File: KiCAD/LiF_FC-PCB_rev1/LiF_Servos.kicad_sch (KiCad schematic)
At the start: 4 parts, among them J37 SRV 3V3_{EN}, J38 Servo A, J39 Servo B

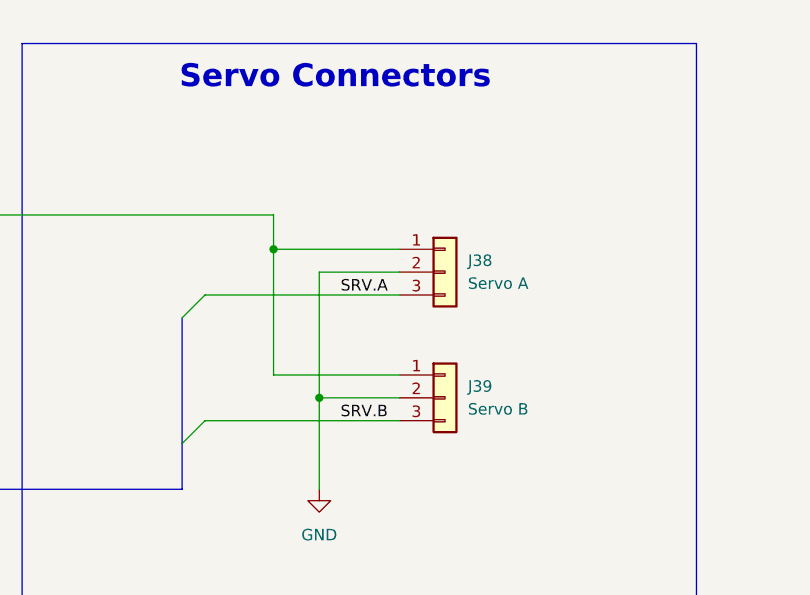
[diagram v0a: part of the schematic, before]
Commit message: fixing ERC bugs on schematic. Only MCU left
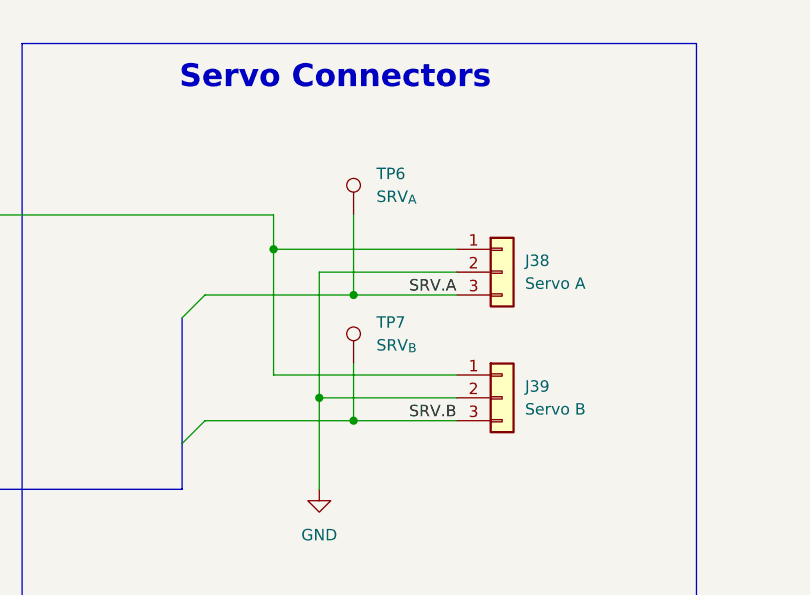
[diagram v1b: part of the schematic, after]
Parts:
- added TP6: SRV_{A}, TestPoint:TestPoint_Bridge_Pitch2.54mm_Drill1.0mm, symbol Connector:TestPoint
- added TP7: SRV_{B}, TestPoint:TestPoint_Bridge_Pitch2.54mm_Drill1.0mm, symbol Connector:TestPoint
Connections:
- net SRV.A: now also TP6.1
- net SRV.B: now also TP7.1
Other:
- moved on the sheet: J38, J39

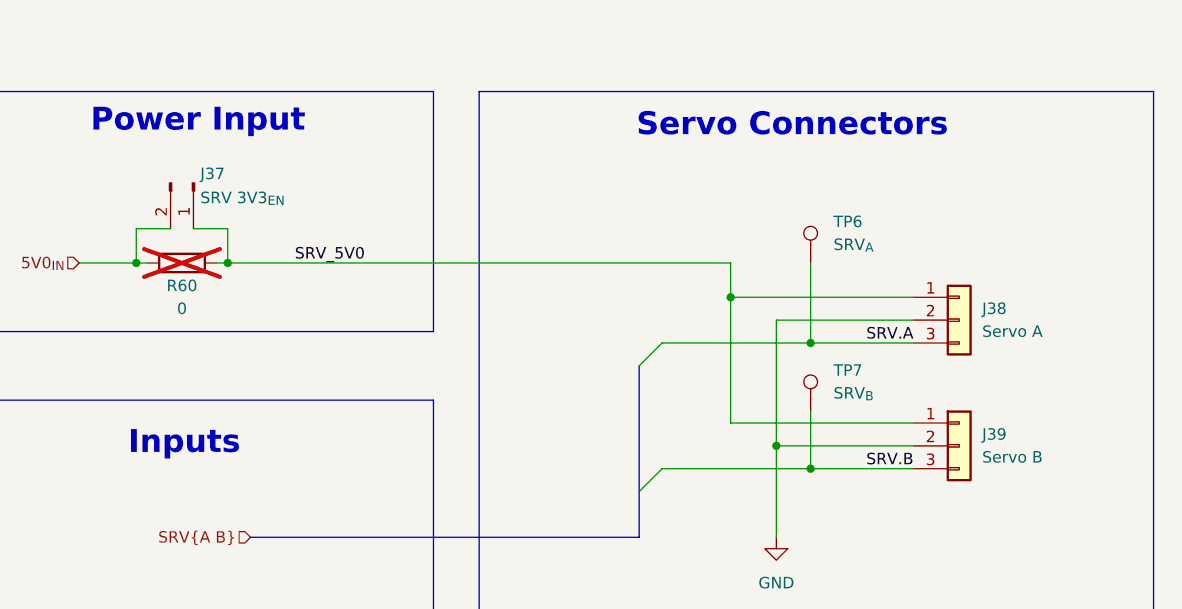
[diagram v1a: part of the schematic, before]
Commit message: Added MCU pinout, shanged shift registers to GPIO expanders to save pins on MCU
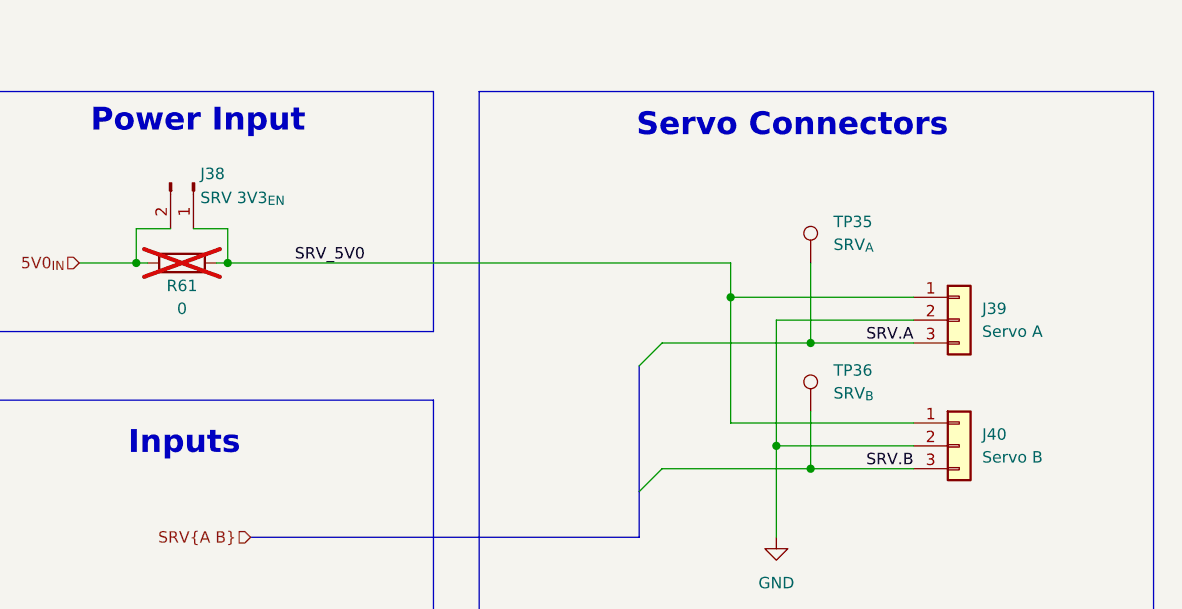
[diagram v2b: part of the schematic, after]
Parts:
- renumbered J37 to J38, J38 to J39, J39 to J40, R60 to R61, TP6 to TP35, TP7 to TP36
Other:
- title: (none) -> Lithium Firefly Custom FC/CC PCB
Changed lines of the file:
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@@
 	(paper "A4")
 	(title_block
+		(title "Lithium Firefly Custom FC/CC PCB")
+		(date "2026-07-12")
 		(rev "1")
 		(company "Lithium Firefly Team")
+		(comment 1 "Designed by MR")
 		(comment 2 "Verified by MR")
 	)
@@
 		(dnp no)
 		(fields_autoplaced yes)
-		(property "Reference" "J39"
+		(property "Reference" "J40"
 			(at 166.37 110.4899 0)
 			(effects
@@
 			(project "LiF_FC-PCB_rev1"
 				(path "/9e3e8da7-e506-46c9-90e5-307e4ad30d29/a8743cf2-df76-4292-9b13-dfab84e92b69"
-					(reference "J39")
+					(reference "J40")
 					(unit 1)
 				)
@@
 		(on_board yes)
 		(dnp no)
-		(property "Reference" "TP6"
+		(property "Reference" "TP35"
 			(at 149.86 86.8679 0)
 			(effects
@@
 			(project "LiF_FC-PCB_rev1"
 				(path "/9e3e8da7-e506-46c9-90e5-307e4ad30d29/a8743cf2-df76-4292-9b13-dfab84e92b69"
-					(reference "TP6")
+					(reference "TP35")
 					(unit 1)
 				)
@@
 		(on_board yes)
 		(dnp no)
-		(property "Reference" "J37"
+		(property "Reference" "J38"
 			(at 79.502 81.534 90)
 			(effects
@@
 			(project "LiF_FC-PCB_rev1"
 				(path "/9e3e8da7-e506-46c9-90e5-307e4ad30d29/a8743cf2-df76-4292-9b13-dfab84e92b69"
-					(reference "J37")
+					(reference "J38")
 					(unit 1)
 				)
@@
 		(dnp no)
 		(fields_autoplaced yes)
-		(property "Reference" "J38"
+		(property "Reference" "J39"
 			(at 166.37 96.5199 0)
 			(effects
@@
 			(project ""
 				(path "/9e3e8da7-e506-46c9-90e5-307e4ad30d29/a8743cf2-df76-4292-9b13-dfab84e92b69"
-					(reference "J38")
+					(reference "J39")
 					(unit 1)
 				)
@@
 		(dnp no)
 		(fields_autoplaced yes)
-		(property "Reference" "#PWR0110"
+		(property "Reference" "#PWR0114"
 			(at 143.51 128.27 0)
 			(effects
@@
 			(project "LiF_FC-PCB_rev1"
 				(path "/9e3e8da7-e506-46c9-90e5-307e4ad30d29/a8743cf2-df76-4292-9b13-dfab84e92b69"
-					(reference "#PWR0110")
+					(reference "#PWR0114")
 					(unit 1)
 				)
@@
 		(on_board yes)
 		(dnp yes)
-		(property "Reference" "R60"
+		(property "Reference" "R61"
 			(at 77.47 93.98 90)
 			(effects
@@
 			(project "LiF_FC-PCB_rev1"
 				(path "/9e3e8da7-e506-46c9-90e5-307e4ad30d29/a8743cf2-df76-4292-9b13-dfab84e92b69"
-					(reference "R60")
+					(reference "R61")
 					(unit 1)
 				)
@@
 		(on_board yes)
 		(dnp no)
-		(property "Reference" "TP7"
+		(property "Reference" "TP36"
 			(at 149.86 103.3779 0)
 			(effects
@@
 			(project "LiF_FC-PCB_rev1"
 				(path "/9e3e8da7-e506-46c9-90e5-307e4ad30d29/a8743cf2-df76-4292-9b13-dfab84e92b69"
-					(reference "TP7")
+					(reference "TP36")
 					(unit 1)
 				)

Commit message: Finalized schematic diagram. Only needs formatting fixes and resistor component sourcing info
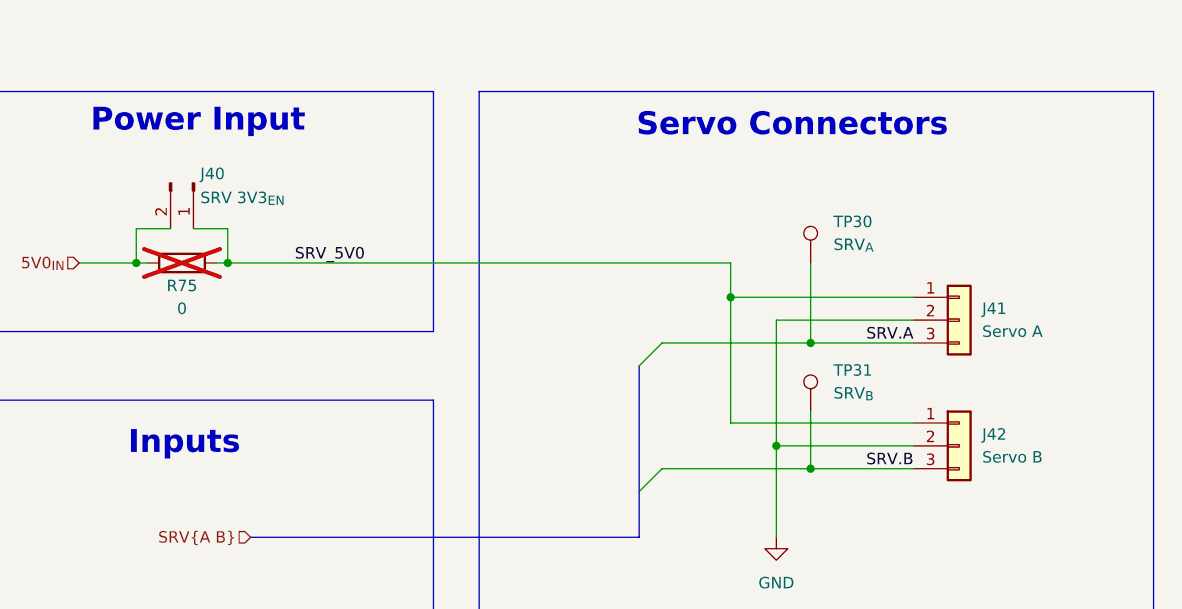
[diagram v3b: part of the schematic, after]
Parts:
- renumbered J38 to J40, J39 to J41, J40 to J42, R61 to R75, TP35 to TP30, TP36 to TP31
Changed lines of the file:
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@@
 		(dnp no)
 		(fields_autoplaced yes)
-		(property "Reference" "J40"
+		(property "Reference" "J42"
 			(at 166.37 110.4899 0)
 			(effects
@@
 			(project "LiF_FC-PCB_rev1"
 				(path "/9e3e8da7-e506-46c9-90e5-307e4ad30d29/a8743cf2-df76-4292-9b13-dfab84e92b69"
-					(reference "J40")
+					(reference "J42")
 					(unit 1)
 				)
@@
 		(on_board yes)
 		(dnp no)
-		(property "Reference" "TP35"
+		(property "Reference" "TP30"
 			(at 149.86 86.8679 0)
 			(effects
@@
 			(project "LiF_FC-PCB_rev1"
 				(path "/9e3e8da7-e506-46c9-90e5-307e4ad30d29/a8743cf2-df76-4292-9b13-dfab84e92b69"
-					(reference "TP35")
+					(reference "TP30")
 					(unit 1)
 				)
@@
 		(on_board yes)
 		(dnp no)
-		(property "Reference" "J38"
+		(property "Reference" "J40"
 			(at 79.502 81.534 90)
 			(effects
@@
 			(project "LiF_FC-PCB_rev1"
 				(path "/9e3e8da7-e506-46c9-90e5-307e4ad30d29/a8743cf2-df76-4292-9b13-dfab84e92b69"
-					(reference "J38")
+					(reference "J40")
 					(unit 1)
 				)
@@
 		(dnp no)
 		(fields_autoplaced yes)
-		(property "Reference" "J39"
+		(property "Reference" "J41"
 			(at 166.37 96.5199 0)
 			(effects
@@
 			(project ""
 				(path "/9e3e8da7-e506-46c9-90e5-307e4ad30d29/a8743cf2-df76-4292-9b13-dfab84e92b69"
-					(reference "J39")
+					(reference "J41")
 					(unit 1)
 				)
@@
 		(dnp no)
 		(fields_autoplaced yes)
-		(property "Reference" "#PWR0114"
+		(property "Reference" "#PWR0113"
 			(at 143.51 128.27 0)
 			(effects
@@
 			(project "LiF_FC-PCB_rev1"
 				(path "/9e3e8da7-e506-46c9-90e5-307e4ad30d29/a8743cf2-df76-4292-9b13-dfab84e92b69"
-					(reference "#PWR0114")
+					(reference "#PWR0113")
 					(unit 1)
 				)
@@
 		(on_board yes)
 		(dnp yes)
-		(property "Reference" "R61"
+		(property "Reference" "R75"
 			(at 77.47 93.98 90)
 			(effects
@@
 			(project "LiF_FC-PCB_rev1"
 				(path "/9e3e8da7-e506-46c9-90e5-307e4ad30d29/a8743cf2-df76-4292-9b13-dfab84e92b69"
-					(reference "R61")
+					(reference "R75")
 					(unit 1)
 				)
@@
 		(on_board yes)
 		(dnp no)
-		(property "Reference" "TP36"
+		(property "Reference" "TP31"
 			(at 149.86 103.3779 0)
 			(effects
@@
 			(project "LiF_FC-PCB_rev1"
 				(path "/9e3e8da7-e506-46c9-90e5-307e4ad30d29/a8743cf2-df76-4292-9b13-dfab84e92b69"
-					(reference "TP36")
-					(unit 1)
-				)
+					(reference "TP31")
+					(unit 1)
+				)

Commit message: added door limit switch and fixed I2C pull up resistors
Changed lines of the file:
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@@
 	(rectangle
 		(start 53.34 72.39)
-		(end 105.41 99.06)
+		(end 105.41 102.87)
 		(stroke
 			(width 0)

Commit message: set up board configuration and started routing PCB
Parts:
- TP30, TP31: footprint TestPoint:TestPoint_Bridge_Pitch2.54mm_Drill1.0mm -> TestPoint:TestPoint_Loop_D1.80mm_Drill1.0mm_Beaded
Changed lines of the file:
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@@
 			)
 		)
-		(property "Footprint" "TestPoint:TestPoint_Bridge_Pitch2.54mm_Drill1.0mm"
+		(property "Footprint" "TestPoint:TestPoint_Loop_D1.80mm_Drill1.0mm_Beaded"
 			(at 152.4 91.44 0)
 			(effects
@@
 			)
 		)
-		(property "Footprint" "TestPoint:TestPoint_Bridge_Pitch2.54mm_Drill1.0mm"
+		(property "Footprint" "TestPoint:TestPoint_Loop_D1.80mm_Drill1.0mm_Beaded"
 			(at 152.4 107.95 0)
 			(effects

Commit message: backup before leaving school
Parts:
- J40: footprint Connector_PinHeader_2.54mm:PinHeader_1x02_P2.54mm_Vertical -> Connector_PinHeader_2.54mm:PinHeader_1x02_P2.54mm_Vertical_SMD_Pin1Left
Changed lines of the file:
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@@
 			)
 		)
-		(property "Footprint" "Connector_PinHeader_2.54mm:PinHeader_1x02_P2.54mm_Vertical"
+		(property "Footprint" "Connector_PinHeader_2.54mm:PinHeader_1x02_P2.54mm_Vertical_SMD_Pin1Left"
 			(at 78.74 82.55 0)
 			(effects

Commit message: Created new KiCAD project for IO PCB, moved relevant components there, saving backup before reannotating the Service PCB schematics
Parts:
- J40: now not fitted; now left out of the parts list

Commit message: backup before redoing the analog section
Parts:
- renumbered J40 to J42, J41 to J43, J42 to J44, R75 to R66
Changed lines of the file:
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@@
 		(dnp no)
 		(fields_autoplaced yes)
-		(property "Reference" "J42"
+		(property "Reference" "J44"
 			(at 166.37 110.4899 0)
 			(effects
@@
 			(project "LiF_FC-PCB_rev1"
 				(path "/9e3e8da7-e506-46c9-90e5-307e4ad30d29/a8743cf2-df76-4292-9b13-dfab84e92b69"
-					(reference "J42")
+					(reference "J44")
 					(unit 1)
 				)
@@
 		(on_board no)
 		(dnp yes)
-		(property "Reference" "J40"
+		(property "Reference" "J42"
 			(at 79.502 81.534 90)
 			(effects
@@
 			(project "LiF_FC-PCB_rev1"
 				(path "/9e3e8da7-e506-46c9-90e5-307e4ad30d29/a8743cf2-df76-4292-9b13-dfab84e92b69"
-					(reference "J40")
+					(reference "J42")
 					(unit 1)
 				)
@@
 		(dnp no)
 		(fields_autoplaced yes)
-		(property "Reference" "J41"
+		(property "Reference" "J43"
 			(at 166.37 96.5199 0)
 			(effects
@@
 			(project ""
 				(path "/9e3e8da7-e506-46c9-90e5-307e4ad30d29/a8743cf2-df76-4292-9b13-dfab84e92b69"
-					(reference "J41")
+					(reference "J43")
 					(unit 1)
 				)
@@
 		(dnp no)
 		(fields_autoplaced yes)
-		(property "Reference" "#PWR0113"
+		(property "Reference" "#PWR093"
 			(at 143.51 128.27 0)
 			(effects
@@
 			(project "LiF_FC-PCB_rev1"
 				(path "/9e3e8da7-e506-46c9-90e5-307e4ad30d29/a8743cf2-df76-4292-9b13-dfab84e92b69"
-					(reference "#PWR0113")
+					(reference "#PWR093")
 					(unit 1)
 				)
@@
 		(on_board yes)
 		(dnp yes)
-		(property "Reference" "R75"
+		(property "Reference" "R66"
 			(at 77.47 93.98 90)
 			(effects
@@
 			(project "LiF_FC-PCB_rev1"
 				(path "/9e3e8da7-e506-46c9-90e5-307e4ad30d29/a8743cf2-df76-4292-9b13-dfab84e92b69"
-					(reference "R75")
+					(reference "R66")
 					(unit 1)
 				)
